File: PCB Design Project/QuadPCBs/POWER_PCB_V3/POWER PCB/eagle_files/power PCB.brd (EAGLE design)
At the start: 35 x 35 mm, 33 parts, among them U2 LM2678DX-5.0

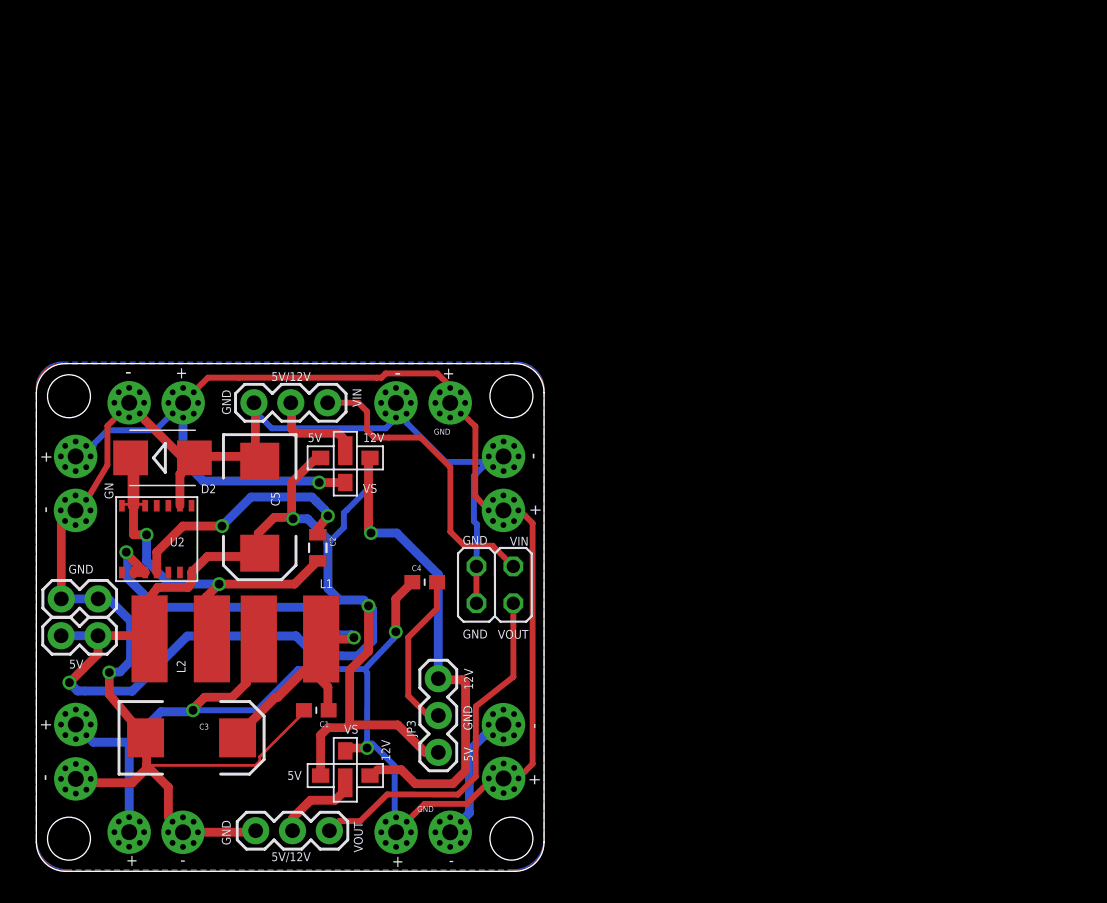
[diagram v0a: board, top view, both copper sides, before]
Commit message: modified the Schematic
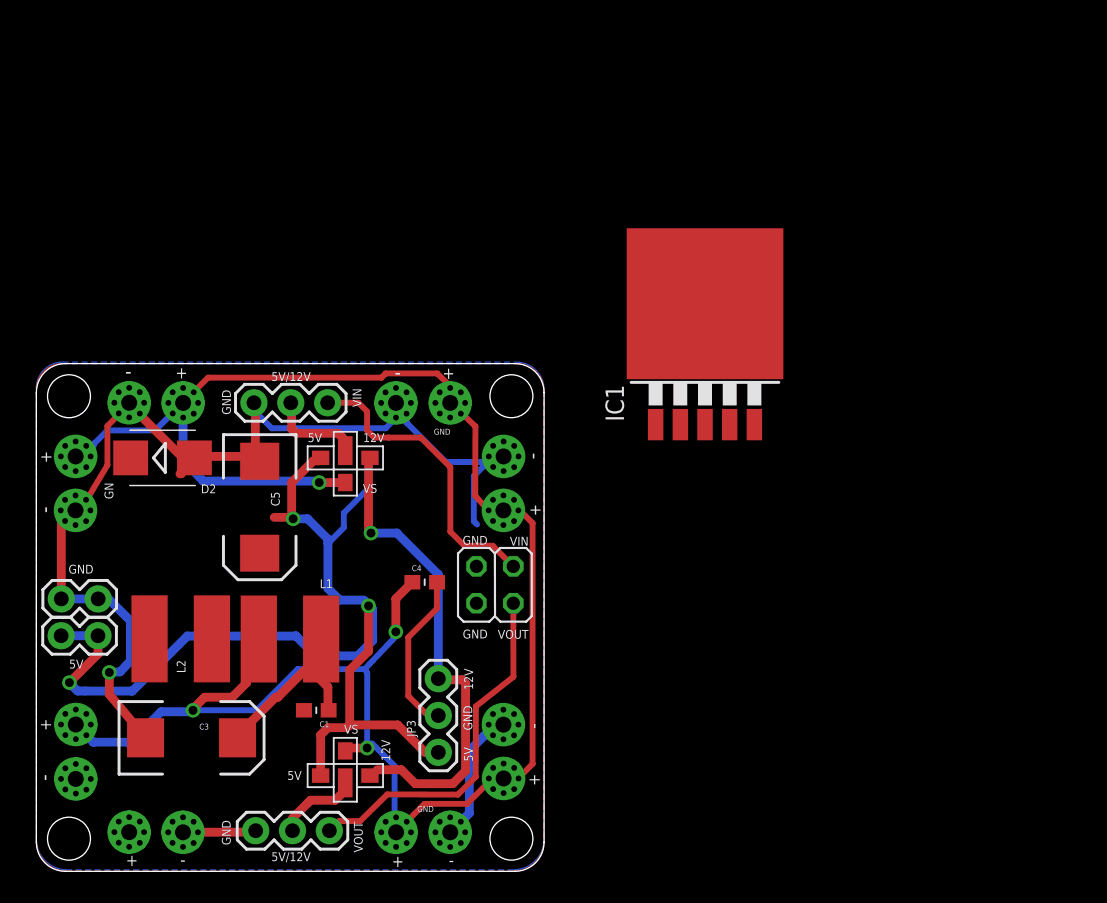
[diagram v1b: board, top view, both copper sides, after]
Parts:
- removed C2: 0.01uF, SparkFun-Capacitors:0805
- removed U2: LM2678DX-5.0, LM2678SDX-5.0:VSON-14
- added IC1: LM2596S, national-semiconductor:TO263-5
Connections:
- new net N$2: IC1.1
- net 5V: now also D2.C; no longer C5.A, L2.2, U2.7
- net GND: now also IC1.3, IC1.5; no longer U2.9
- net N$1: now also IC1.2; no longer C2.2, D2.C, U2.12, U2.13, U2.14
- net N$3: now also IC1.4, L2.2; no longer C2.1, U2.4
- net N$4: no longer U2.2, U2.3
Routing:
- net GND: track 174.3 -> 140.4 mm
- net N$1: track 28.1 -> 0.00 mm, vias 2 -> 0
- net N$4: track 38.6 -> 12.7 mm, vias 2 -> 0
- net VS: track 199.0 -> 174.9 mm
- net 5V: track 96.3 -> 77.0 mm
- net N$3: track 16.9 -> 0.00 mm, vias 2 -> 0

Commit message: layout of component
problem with input cap for the switching regulator
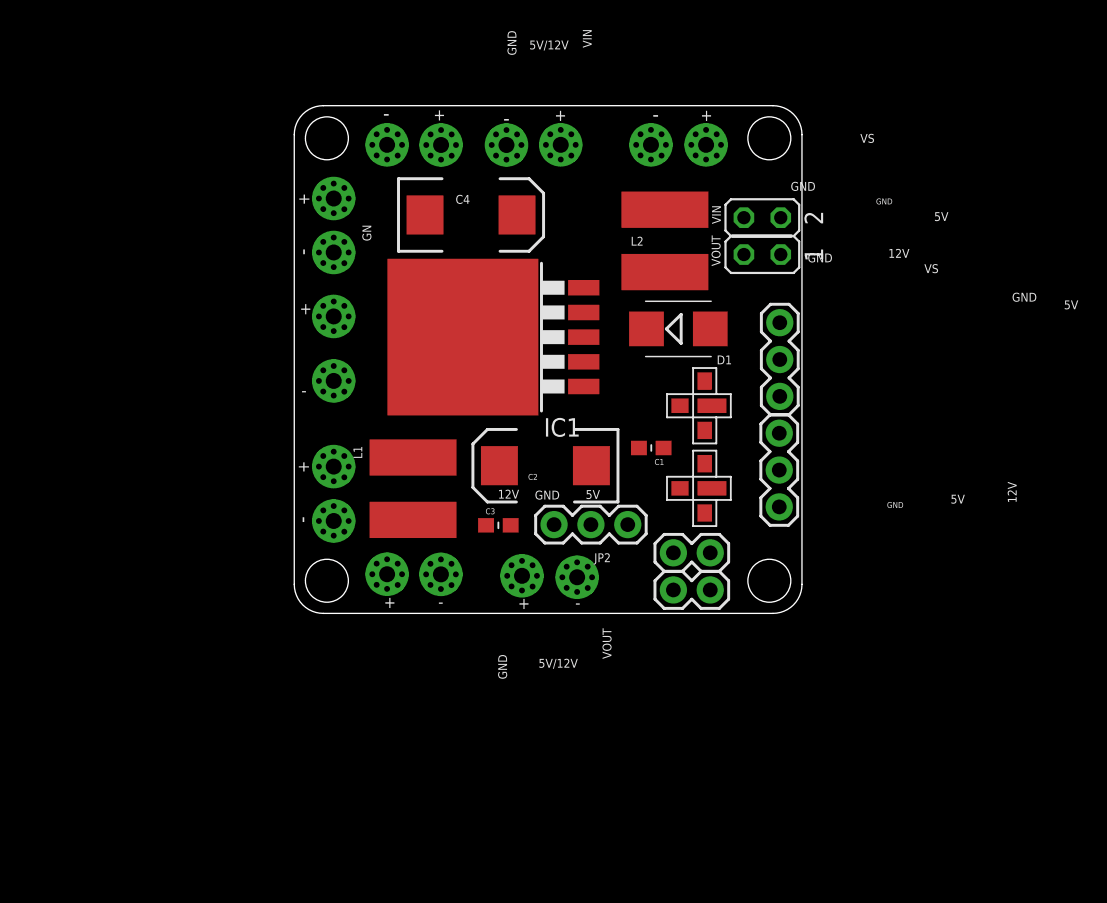
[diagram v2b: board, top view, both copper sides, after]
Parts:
- removed C5: 100uF, SparkFun-Capacitors:EIA7343
- removed D2: MBRS130LT3, diode:SMB
- removed PAD17, PAD18, PAD19, PAD20, PAD21, PAD22, PAD23, PAD24: PAD_3MM, PAD_3MM:PAD_3MM
- removed U$1, U$3: 3WAY_SMD_JUMPER, jumper_smd_3way:3WAY_JUMPER
- added C2: 680uF, SparkFun-Capacitors:EIA7343
- added D1: MBRS360, diode:SMB
- added JP6: M02PTH, SparkFun-Connectors:1X02
- added JP7: (no value), SparkFun-Connectors:1X03
- added PAD11, PAD12, PAD13, PAD14, PAD3, PAD4, PAD5, PAD6: PAD_3MM, Power PCB:PAD_3MM
- C3: value 100uF -> 0.1uF; device SparkFun-Capacitors:EIA7343 -> SparkFun-Capacitors:0603-CAP
- C4: value 0.1uF -> 330uF; device SparkFun-Capacitors:0603-CAP -> SparkFun-Capacitors:EIA7343
- JP1: device SparkFun-Connectors:1X03 -> jumper:JP2Q
- JP3: value (none) -> 3WAY_SMD_JUMPER; device SparkFun-Connectors:1X03 -> Power PCB:3WAY_JUMPER
- JP4: value M02PTH -> 3WAY_SMD_JUMPER; device SparkFun-Connectors:1X02 -> Power PCB:3WAY_JUMPER
- JP8: device jumper:JP2Q -> SparkFun-Connectors:1X03
- PAD1, PAD10, PAD15, PAD16, PAD2, PAD7, PAD8, PAD9: device PAD_3MM:PAD_3MM -> Power PCB:PAD_3MM
- moved JP1 50.7 mm to (32.5, 26.3), turned to 90 degrees
- moved PAD8 48.7 mm to (6.68, 32.6)
- moved PAD7 47.2 mm to (10.4, 32.6)
- moved JP4 46.3 mm to (28.6, 14.6), turned to 270 degrees
- moved JP5 44.9 mm to (29.0, 1.90), turned to 180 degrees
- moved L2 43.2 mm to (25.7, 26.0), turned to 90 degrees
- moved PAD16 29.8 mm to (3.00, 16.3)
- moved C1 29.3 mm to (24.9, 11.7)
- moved PAD10 28.8 mm to (28.7, 32.6)
- moved JP8 26.7 mm to (33.8, 20.3), turned to 270 degrees
- moved C3 25.7 mm to (14.4, 6.35)
- moved C4 25.5 mm to (12.5, 27.7)
- moved PAD2 25.2 mm to (3.00, 25.2)
- moved PAD1 25.2 mm to (3.00, 28.9)
- moved PAD9 23.8 mm to (24.9, 32.6)
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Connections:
- removed net N$1: IC1.2, L2.1
- removed net N$2: IC1.1
- removed net N$4: C1.1, C3.A, L1.2
- new net VSF: C2.A, C3.1, IC1.1, JP3.2, JP4.2, L1.2
- net 12V: now also JP2.1, JP3.3, JP4.1; no longer JP3.1, U$1.3, U$3.1
- net 5V: now also C4.A, IC1.4, JP2.3, JP3.1, JP4.3, JP6.1, JP6.2, L2.2; no longer D2.C, JP3.3, JP5.1, JP5.2, U$1.1, U$3.3
- net FPV: now also JP3.4, JP7.2; no longer JP2.2, U$1.4
- net GND: now also C2.C, C3.2, C4.C, D1.A, JP1.1, JP1.2, JP2.2, JP5.1, JP5.2, JP7.1, JP8.3, PAD11.P$1, PAD11.P$2, PAD11.P$3, PAD11.P$4, PAD11.P$5, PAD11.P$6, PAD11.P$7, PAD11.P$8, PAD11.P$9, PAD14.P$1, PAD14.P$2, PAD14.P$3, PAD14.P$4, PAD14.P$5, PAD14.P$6, PAD14.P$7, PAD14.P$8, PAD14.P$9, PAD16.P$1, PAD16.P$2, PAD16.P$3, PAD16.P$4, PAD16.P$5, PAD16.P$6, PAD16.P$7, PAD16.P$8, PAD16.P$9, PAD4.P$1, PAD4.P$2, PAD4.P$3, PAD4.P$4, PAD4.P$5, PAD4.P$6, PAD4.P$7, PAD4.P$8, PAD4.P$9, PAD6.P$1, PAD6.P$2, PAD6.P$3, PAD6.P$4, PAD6.P$5, PAD6.P$6, PAD6.P$7, PAD6.P$8, PAD6.P$9; no longer C3.C, C4.2, C5.C, D2.A, JP1.3, JP2.1, JP3.2, JP4.1, JP4.2, JP8.1, JP8.2, PAD15.P$1, PAD15.P$2, PAD15.P$3, PAD15.P$4, PAD15.P$5, PAD15.P$6, PAD15.P$7, PAD15.P$8, PAD15.P$9, PAD18.P$1, PAD18.P$2, PAD18.P$3, PAD18.P$4, PAD18.P$5, PAD18.P$6, PAD18.P$7, PAD18.P$8, PAD18.P$9, PAD20.P$1, PAD20.P$2, PAD20.P$3, PAD20.P$4, PAD20.P$5, PAD20.P$6, PAD20.P$7, PAD20.P$8, PAD20.P$9, PAD22.P$1, PAD22.P$2, PAD22.P$3, PAD22.P$4, PAD22.P$5, PAD22.P$6, PAD22.P$7, PAD22.P$8, PAD22.P$9, PAD23.P$1, PAD23.P$2, PAD23.P$3, PAD23.P$4, PAD23.P$5, PAD23.P$6, PAD23.P$7, PAD23.P$8, PAD23.P$9
- net N$3: now also D1.C, IC1.2, L2.1; no longer IC1.4, L2.2
- net VIN: now also JP1.4, JP7.3; no longer JP2.3, JP8.4
- net VOUT: now also JP1.3, JP8.1; no longer JP1.1, JP8.3
- net VS: now also C1.1, PAD12.P$1, PAD12.P$2, PAD12.P$3, PAD12.P$4, PAD12.P$5, PAD12.P$6, PAD12.P$7, PAD12.P$8, PAD12.P$9, PAD13.P$1, PAD13.P$2, PAD13.P$3, PAD13.P$4, PAD13.P$5, PAD13.P$6, PAD13.P$7, PAD13.P$8, PAD13.P$9, PAD15.P$1, PAD15.P$2, PAD15.P$3, PAD15.P$4, PAD15.P$5, PAD15.P$6, PAD15.P$7, PAD15.P$8, PAD15.P$9, PAD3.P$1, PAD3.P$2, PAD3.P$3, PAD3.P$4, PAD3.P$5, PAD3.P$6, PAD3.P$7, PAD3.P$8, PAD3.P$9, PAD5.P$1, PAD5.P$2, PAD5.P$3, PAD5.P$4, PAD5.P$5, PAD5.P$6, PAD5.P$7, PAD5.P$8, PAD5.P$9; no longer C4.1, PAD16.P$1, PAD16.P$2, PAD16.P$3, PAD16.P$4, PAD16.P$5, PAD16.P$6, PAD16.P$7, PAD16.P$8, PAD16.P$9, PAD17.P$1, PAD17.P$2, PAD17.P$3, PAD17.P$4, PAD17.P$5, PAD17.P$6, PAD17.P$7, PAD17.P$8, PAD17.P$9, PAD19.P$1, PAD19.P$2, PAD19.P$3, PAD19.P$4, PAD19.P$5, PAD19.P$6, PAD19.P$7, PAD19.P$8, PAD19.P$9, PAD21.P$1, PAD21.P$2, PAD21.P$3, PAD21.P$4, PAD21.P$5, PAD21.P$6, PAD21.P$7, PAD21.P$8, PAD21.P$9, PAD24.P$1, PAD24.P$2, PAD24.P$3, PAD24.P$4, PAD24.P$5, PAD24.P$6, PAD24.P$7, PAD24.P$8, PAD24.P$9, U$1.2, U$3.2
- net VTX: now also JP4.4, JP8.2; no longer JP1.2, U$3.4
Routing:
- net VS: track 174.9 -> 0.00 mm, vias 4 -> 0
- net GND: track 140.4 -> 0.00 mm, vias 1 -> 0
- net 5V: track 77.0 -> 0.00 mm, vias 3 -> 0
- net 12V: track 34.0 -> 0.00 mm, vias 1 -> 0
- net VOUT: track 24.8 -> 0.00 mm
- net VIN: track 20.8 -> 0.00 mm
- net N$4: track 12.7 -> 0.00 mm
- net FPV: track 6.76 -> 0.00 mm
- net VTX: track 6.04 -> 0.00 mm
- removed copper zone on layer 1, net GND
- removed copper zone on layer 16, net VS

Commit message: finished PCB design
Change regulator back to LM7689 but in TO-203-7 package
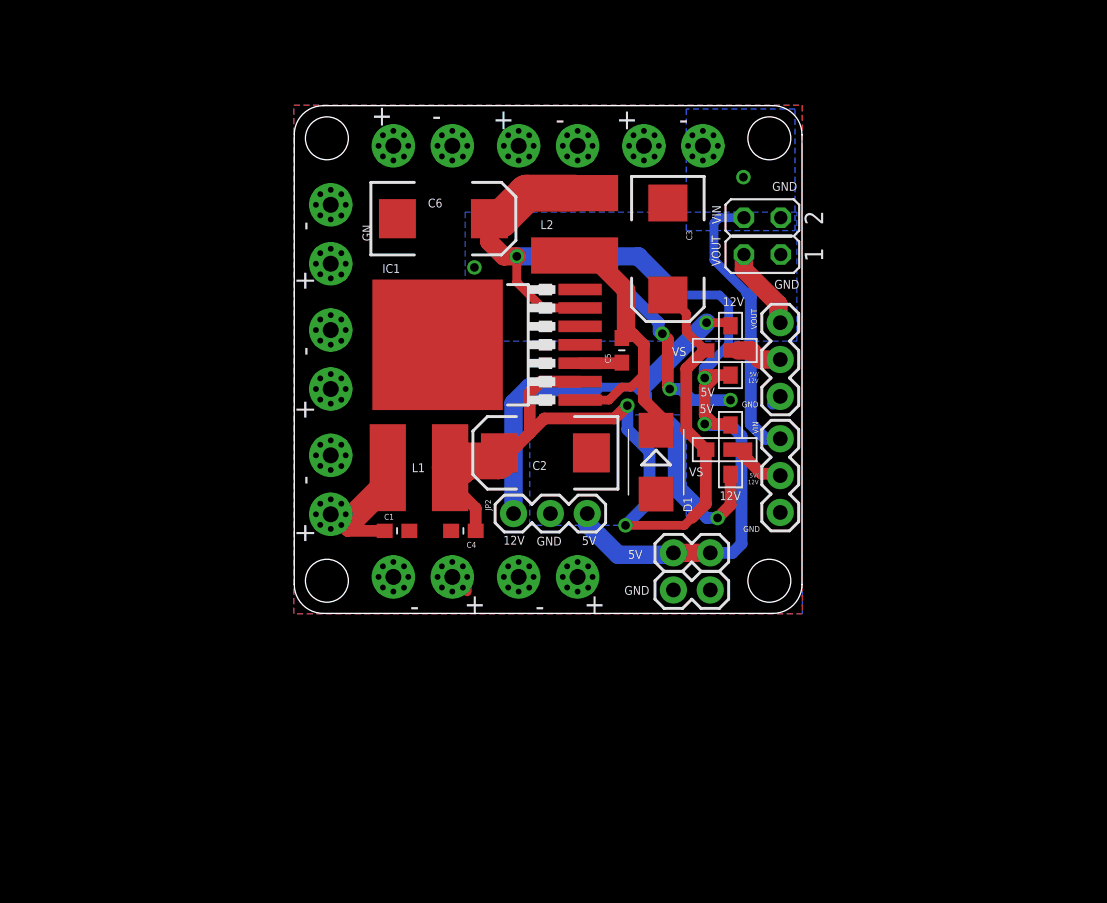
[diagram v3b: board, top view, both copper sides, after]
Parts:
- added C5: 0.01uF, SparkFun-Capacitors:0603-CAP
- added C6: 330uF, SparkFun-Capacitors:EIA7343
- C2: value 680uF -> 100uF; device SparkFun-Capacitors:EIA7343 -> Power PCB:EIA7343
- C3: value 0.1uF -> 100uF; device SparkFun-Capacitors:0603-CAP -> Power PCB:EIA7343
- C4: value 330uF -> 0.1uF; device SparkFun-Capacitors:EIA7343 -> SparkFun-Capacitors:0603-CAP
- IC1: value LM2596S -> LM2678SX-5.0; device national-semiconductor:TO263-5 -> Power PCB:P-TO263-7-1
- moved C3 22.3 mm to (26.0, 25.4), turned to 270 degrees
- moved C4 21.8 mm to (11.9, 5.97), turned to 180 degrees
- moved C1 18.4 mm to (7.37, 5.97), turned to 0 degrees
- moved D1 9.31 mm to (25.2, 10.7), turned to 270 degrees
- moved L2 6.33 mm to (19.4, 27.1)
- moved PAD13 5.01 mm to (2.79, 15.7)
- moved PAD6 4.90 mm to (19.8, 32.5)
- moved PAD4 4.53 mm to (2.79, 11.2)
- moved PAD1 4.50 mm to (2.79, 24.4)
- moved PAD15 4.50 mm to (11.2, 2.79)
- moved PAD8 4.50 mm to (11.2, 32.5)
- moved PAD10 4.29 mm to (24.4, 32.5)
- moved JP4 4.20 mm to (30.4, 18.4)
- moved PAD11 4.03 mm to (15.7, 2.79)
- moved PAD12 3.83 mm to (19.8, 2.79)
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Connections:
- new net N$1: C5.1, IC1.3
- net 5V: now also C6.A, IC1.6; no longer C4.A, IC1.4
- net GND: now also C3.C, C4.2, C6.C, IC1.4, IC1.TH; no longer C3.2, C4.C, IC1.3, IC1.5
- net N$3: now also C5.2, IC1.1; no longer IC1.2
- net VSF: now also C3.A, C4.1, IC1.2; no longer C3.1, IC1.1
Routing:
- net 5V: track 0.00 -> 72.3 mm, vias 0 -> 3
- net VSF: track 0.00 -> 58.6 mm, vias 0 -> 2
- net 12V: track 0.00 -> 39.9 mm, vias 0 -> 2
- net N$3: track 0.00 -> 22.2 mm
- net VIN: track 0.00 -> 19.6 mm
- net GND: track 0.00 -> 12.9 mm, vias 0 -> 5
- net VS: track 0.00 -> 11.3 mm
- net VOUT: track 0.00 -> 5.75 mm
- net FPV: track 0.00 -> 3.67 mm
- net VTX: track 0.00 -> 3.19 mm
- net N$1: track 0.00 -> 2.89 mm
- added copper zone on layer 1, net GND
- added copper zone on layer 16, net GND
- added copper zone on layer 16, net VS
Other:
- board text added: "5V/ 12V"
- board text removed: "5V/12V"
